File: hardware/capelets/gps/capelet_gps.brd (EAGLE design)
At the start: 54.6 x 31.1 mm, 8 parts, among them IC1 SAM-M8Q, P1 SHPRD_CPLT_G, T1 SI2374DSSOT23-VSHAY

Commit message: hardware: gps capelet: added component values and BOM
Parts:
- C1: value (none) -> 22u
- C2, C3: value (none) -> 0.1u
- R1: value (none) -> 130R
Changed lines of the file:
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@@
 <?xml version="1.0" encoding="utf-8"?>
 <!DOCTYPE eagle SYSTEM "eagle.dtd">
-<eagle version="9.3.2">
+<eagle version="9.4.2">
 <drawing>
 <settings>
@@
 <attribute name="VALUE" x="10.16" y="2.186" size="1.27" layer="27" align="top-center"/>
 </element>
-<element name="R1" library="shepherd" package="RESC2012X65" value="" x="15.24" y="7.62" smashed="yes">
+<element name="R1" library="shepherd" package="RESC2012X65" value="130R" x="15.24" y="7.62" smashed="yes">
 <attribute name="NAME" x="15.24" y="8.8776" size="1.143" layer="25" font="vector" ratio="16" align="bottom-center"/>
 <attribute name="VALUE" x="15.24" y="5.9814" size="1.27" layer="27" align="top-center"/>
 </element>
-<element name="C1" library="shepherd" package="CAPC3225X280" package3d_urn="urn:adsk.eagle:package:4926069/1" value="" x="41.656" y="17.399" smashed="yes" rot="R270">
+<element name="C1" library="shepherd" package="CAPC3225X280" package3d_urn="urn:adsk.eagle:package:4926069/1" value="22u" x="41.656" y="17.399" smashed="yes" rot="R270">
 <attribute name="NAME" x="41.2506" y="14.224" size="1.143" layer="25" font="vector" ratio="16" rot="R270" align="bottom-center"/>
 <attribute name="VALUE" x="39.3944" y="17.399" size="1.27" layer="27" rot="R270" align="top-center"/>
 </element>
-<element name="C2" library="shepherd" package="CAPC2012X145" package3d_urn="urn:adsk.eagle:package:4930364/1" value="" x="38.354" y="17.272" smashed="yes" rot="R270">
+<element name="C2" library="shepherd" package="CAPC2012X145" package3d_urn="urn:adsk.eagle:package:4930364/1" value="0.1u" x="38.354" y="17.272" smashed="yes" rot="R270">
 <attribute name="NAME" x="37.7436" y="14.732" size="1.143" layer="25" font="vector" ratio="16" rot="R270" align="bottom-center"/>
 <attribute name="VALUE" x="36.6784" y="17.272" size="1.27" layer="27" rot="R270" align="top-center"/>
 </element>
-<element name="C3" library="shepherd" package="CAPC2012X145" package3d_urn="urn:adsk.eagle:package:4930364/1" value="" x="28.829" y="29.972" smashed="yes" rot="R180">
+<element name="C3" library="shepherd" package="CAPC2012X145" package3d_urn="urn:adsk.eagle:package:4930364/1" value="0.1u" x="28.829" y="29.972" smashed="yes" rot="R180">
 <attribute name="NAME" x="26.162" y="30.5824" size="1.143" layer="25" font="vector" ratio="16" rot="R180" align="bottom-center"/>
 <attribute name="VALUE" x="28.829" y="31.6476" size="1.27" layer="27" rot="R180" align="top-center"/>

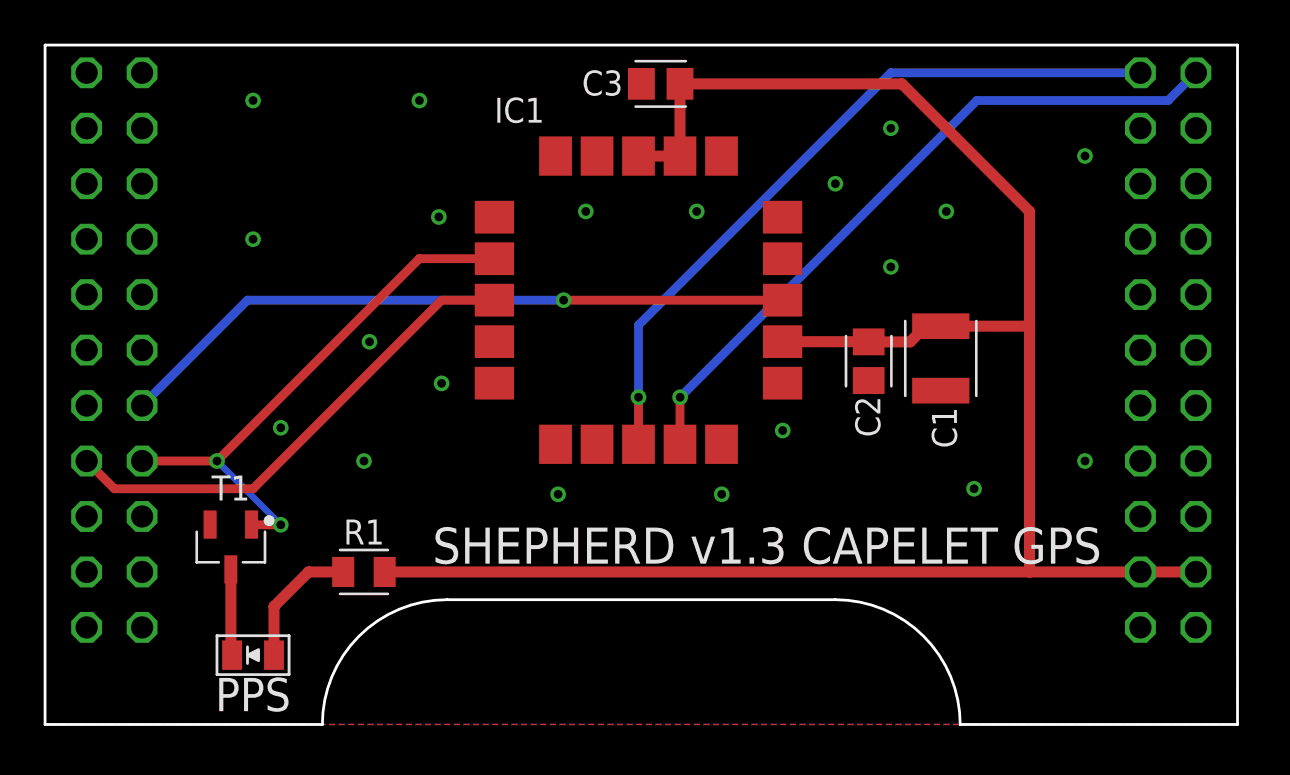
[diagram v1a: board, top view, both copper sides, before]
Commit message: hardware: revised GPS capelet
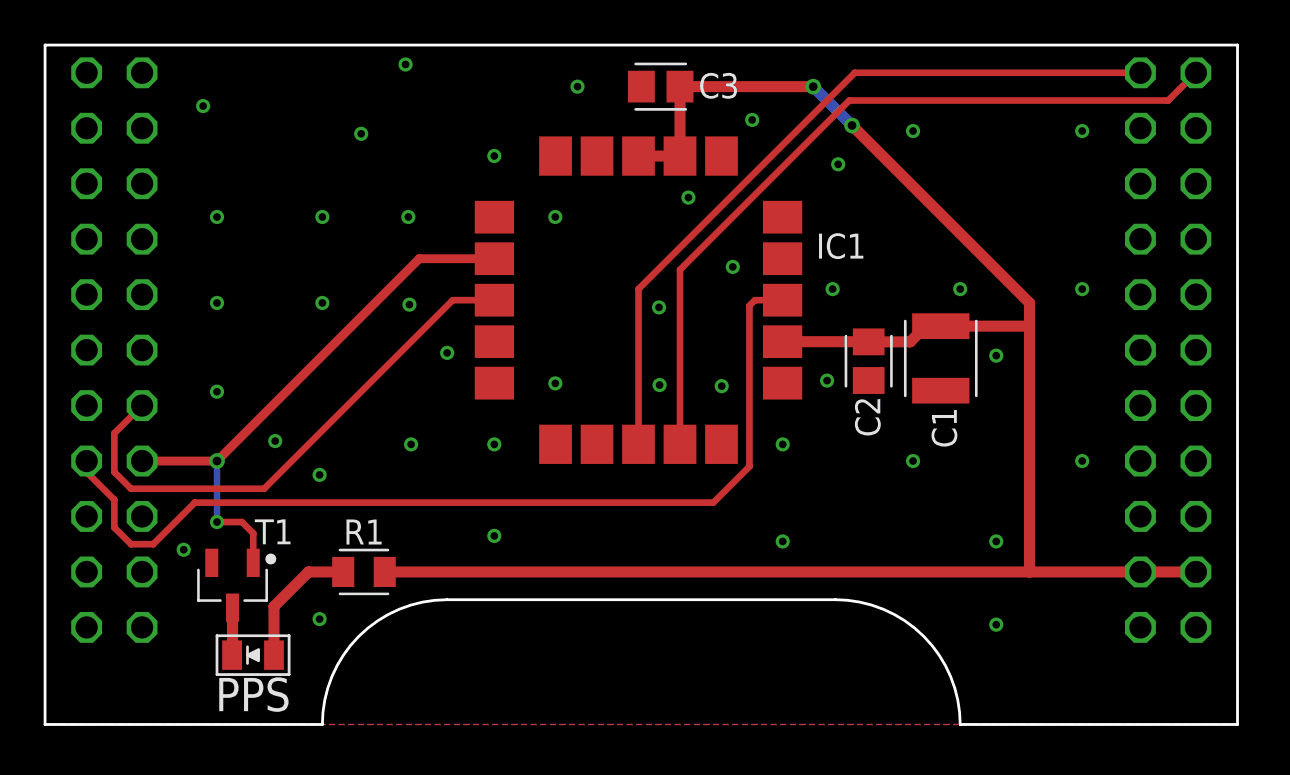
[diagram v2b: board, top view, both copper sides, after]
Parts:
- moved T1 1.75 mm to (9.22, 7.01)
- moved C3 0.13 mm to (28.8, 29.8)
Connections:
- net RESET_N: now also P1.P8$8; no longer P1.P8$9
- net SAFEBOOT_N: now also P1.P8$9; no longer P1.P8$8
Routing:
- net RESET_N: track 31.3 -> 43.4 mm, vias 1 -> 0
- net UART2_TX: track 31.9 -> 35.4 mm, vias 1 -> 0
- net +3V3: track 88.9 -> 86.3 mm, vias 0 -> 2
- net SAFEBOOT_N: track 22.8 -> 24.9 mm
- net N$1: track 3.95 -> 2.18 mm
- net UART2_RX: track 33.2 -> 34.2 mm, vias 1 -> 0
- net TIMEPULSE: track 25.4 -> 26.0 mm
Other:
- board text added: "SHEPHERD v1.5 CAPELET GPS"
- board text removed: "SHEPHERD v1.3 CAPELET GPS"

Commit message: hardware: prepared GPS capelet for professional assembly
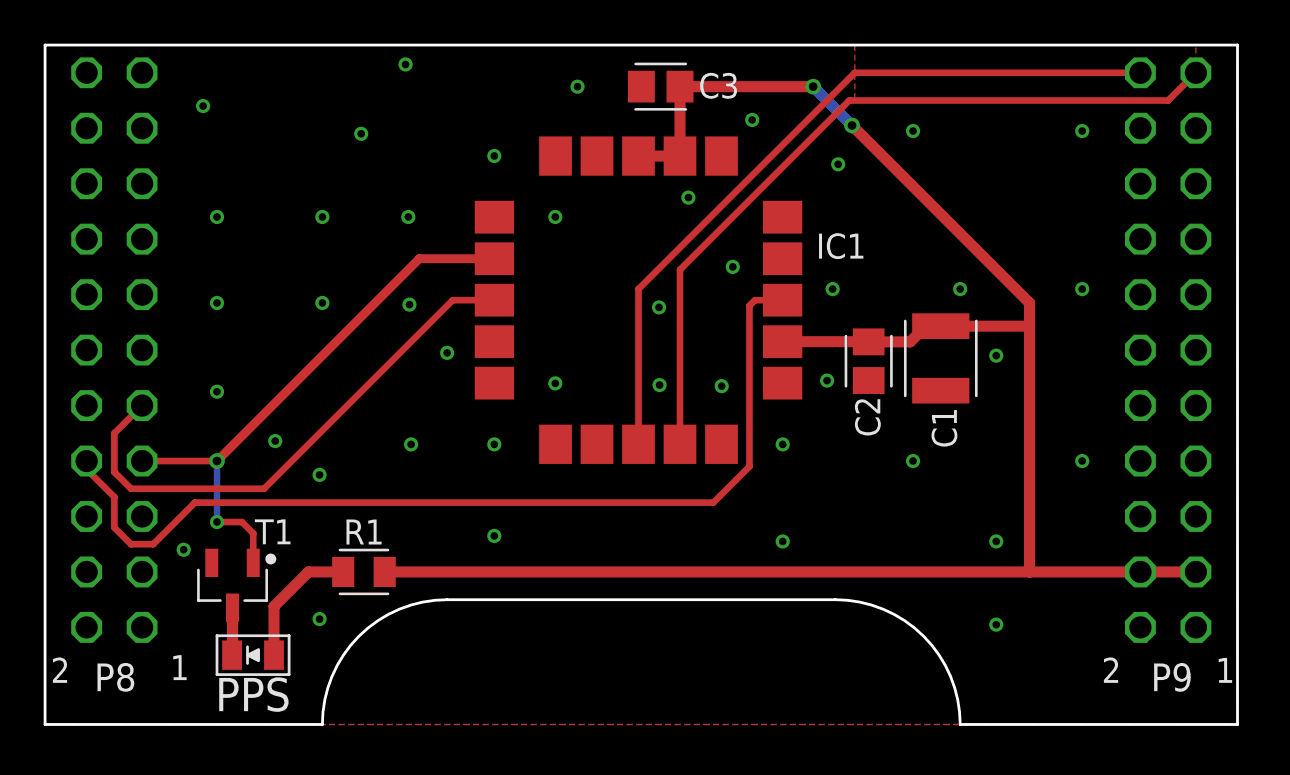
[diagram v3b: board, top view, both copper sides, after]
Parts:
- added P8, P9: (no value), shepherd:2X11
- added U$1, U$2, U$4: (no value), shepherd:REFMARK
- U$3: value SHPRD_CPLT_G -> (none)
- renumbered P1 to U$3
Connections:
- removed net SYS_5V: U$3.P9$7, U$3.P9$8
- removed net VDD_5V: U$3.P9$5, U$3.P9$6
- net +3V3: now also P9.3, P9.4; no longer U$3.P9$3, U$3.P9$4
- net GND: now also P8.1, P8.2, P9.1, P9.2; no longer U$3.P8$1, U$3.P8$2, U$3.P9$1, U$3.P9$2
- net RESET_N: now also P8.8; no longer U$3.P8$8
- net SAFEBOOT_N: now also P8.9; no longer U$3.P8$9
- net TIMEPULSE: now also P8.7; no longer U$3.P8$7
- net UART2_RX: now also P9.22; no longer U$3.P9$22
- net UART2_TX: now also P9.21; no longer U$3.P9$21
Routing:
- added copper zone on layer 1, net KEEPOUT_GND
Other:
- board text added: "1"
- board text added: "2"
- board text added: "P8: pins pointing to bottom, solder on top"
- board text added: "P9: pins pointing to bottom, solder on top"
